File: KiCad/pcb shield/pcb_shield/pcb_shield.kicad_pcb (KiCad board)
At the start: 2 copper layers, 190 x 65 mm, 24 parts, among them J1 , J10 Motor Conn L, J11 Motor Conn R, J12 Endstop X, J13 Endstop Y, J2 , J3 , J4 , J5 , J6 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

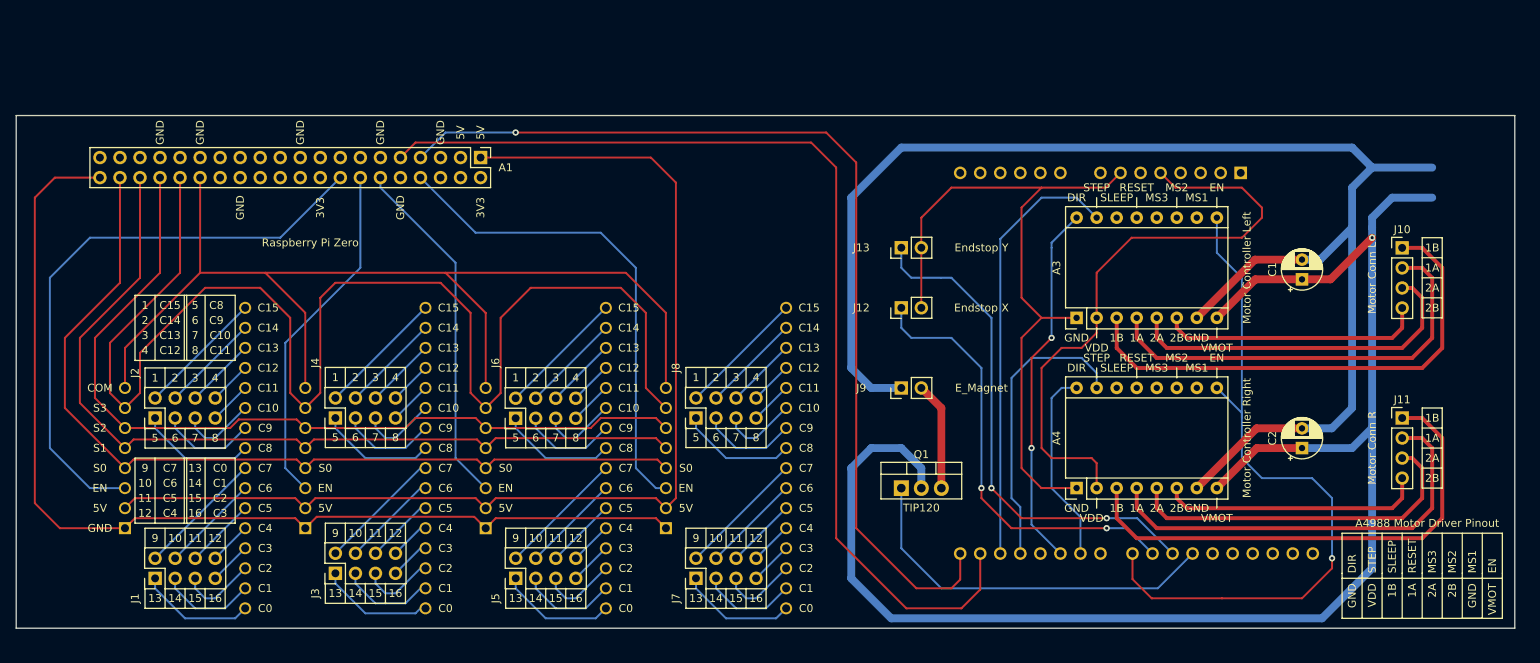
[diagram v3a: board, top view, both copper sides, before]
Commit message: add aditional headers
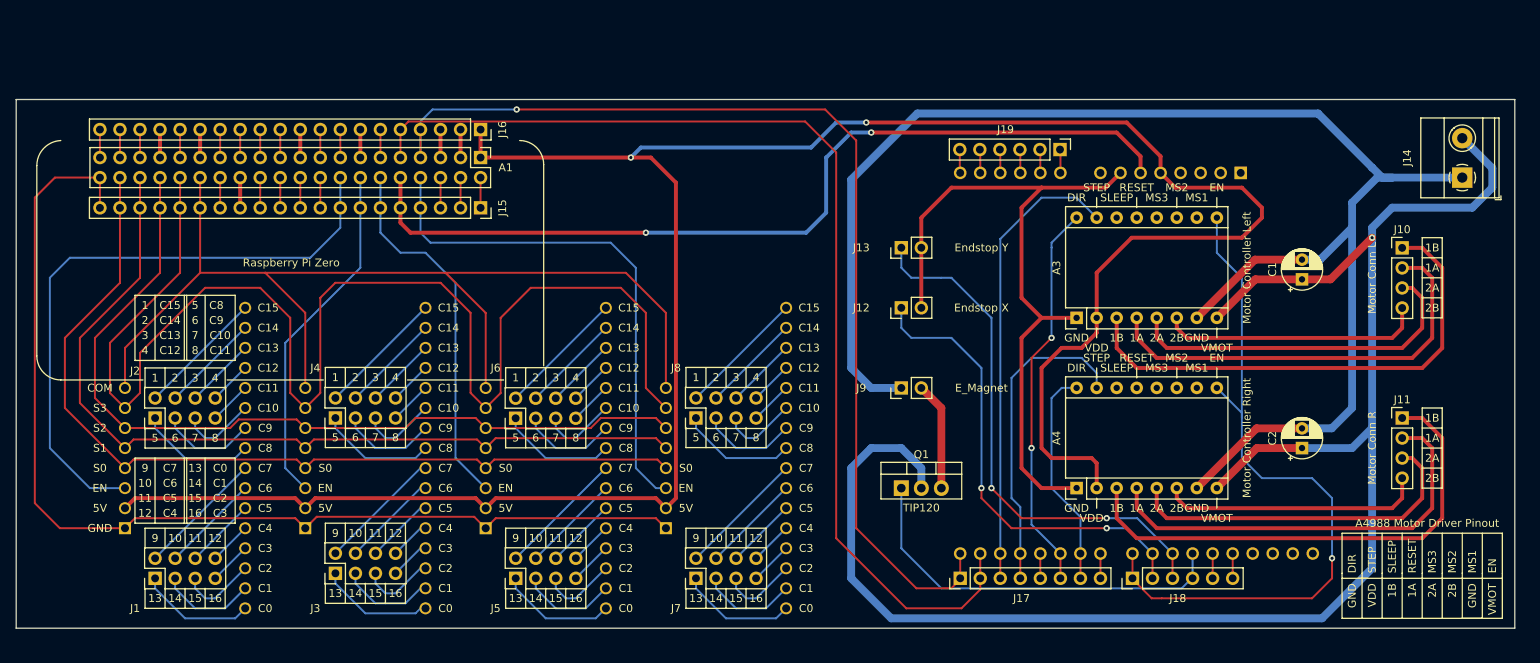
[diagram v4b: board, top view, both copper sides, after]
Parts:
- added J14: Barrel_Jack, TerminalBlock_Phoenix:TerminalBlock_Phoenix_MKDS-1,5-2_1x02_P5.00mm_Horizontal, F.Cu at (243.8, 71.1)
- added J15: Add Conn, Connector_PinSocket_2.54mm:PinSocket_1x20_P2.54mm_Vertical, F.Cu at (119.4, 75.0)
- added J16: Add Conn, Connector_PinSocket_2.54mm:PinSocket_1x20_P2.54mm_Vertical, F.Cu at (119.4, 65.0)
- added J17: Add Conn, Connector_PinHeader_2.54mm:PinHeader_1x08_P2.54mm_Vertical, F.Cu at (180.2, 121.9)
- added J18: Add Conn, Connector_PinHeader_2.54mm:PinHeader_1x06_P2.54mm_Vertical, F.Cu at (202.0, 121.9)
- added J19: Add Conn, Connector_PinHeader_2.54mm:PinHeader_1x06_P2.54mm_Vertical, F.Cu at (192.8, 67.6)
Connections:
- A1 pad 14: unconnected-(A1-Pad14) -> Net-(A1-Pad14)
- A1 pad 26: GND -> Net-(A1-Pad26)
- A1 pad 27: unconnected-(A1-Pad27) -> GND
- A1 pad 34: unconnected-(A1-Pad34) -> Net-(A1-Pad34)
- A2 pad 10: unconnected-(A2-Pad10) -> Net-(A2-Pad10)
- A2 pad 11: unconnected-(A2-Pad11) -> Net-(A2-Pad11)
- A2 pad 12: unconnected-(A2-Pad12) -> Net-(A2-Pad12)
- A2 pad 13: unconnected-(A2-Pad13) -> Net-(A2-Pad13)
- A2 pad 14: unconnected-(A2-Pad14) -> Net-(A2-Pad14)
- A2 pad 19: unconnected-(A2-Pad19) -> Net-(A2-Pad19)
- A2 pad 22: unconnected-(A2-Pad22) -> Net-(A2-Pad22)
- A2 pad 27: unconnected-(A2-Pad27) -> Net-(A2-Pad27)
- A2 pad 28: unconnected-(A2-Pad28) -> Net-(A2-Pad28)
- A2 pad 5: Net-(A4-Pad2) -> 5V
- A2 pad 6: unconnected-(A2-Pad6) -> GND
- A2 pad 9: unconnected-(A2-Pad9) -> Net-(A2-Pad9)
- A3 pad 2: Net-(A4-Pad2) -> 5V
- A4 pad 2: Net-(A4-Pad2) -> 5V
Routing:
- net 5V: track 139.6 -> 296.9 mm, vias 0 -> 2
- net GND: track 0.00 -> 134.4 mm, vias 0 -> 2
- net Net-(A4-Pad2): track 77.3 -> 0.00 mm
- net Net-(A3-Pad8): track 198.1 -> 213.4 mm
- net /14 TXD: track 124.6 -> 134.9 mm
- net Net-(A3-Pad7): track 186.2 -> 196.3 mm
- net 3V3: track 0.00 -> 7.67 mm
- net /18 RXD: track 131.8 -> 137.2 mm
- net Net-(A1-Pad4): track 62.3 -> 66.4 mm
- net SDA: track 0.00 -> 3.83 mm
- net SCL: track 0.00 -> 3.83 mm
- net Net-(A1-Pad14): track 0.00 -> 3.83 mm
- net 9 MISO: track 0.00 -> 3.83 mm
- net 11 SCLK: track 0.00 -> 3.83 mm
- net 10 MOSI: track 0.00 -> 3.83 mm
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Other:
- board size 190 x 65 mm -> 190 x 67 mm
- board text added: "17"
- board text added: "18"
- board text added: "19"
- board text added: "20"
- board text added: "21"
- board text added: "22"
- board text added: "23"
- board text added: "24"
- board text added: "25"
- board text added: "26"
- board text added: "27"
- board text added: "Arduino Uno"
- board text added: "RXD"
- board text added: "SCL"
- board text added: "SDA"
- board text added: "TXD"

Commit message: working on PCB and creating manufacturing files
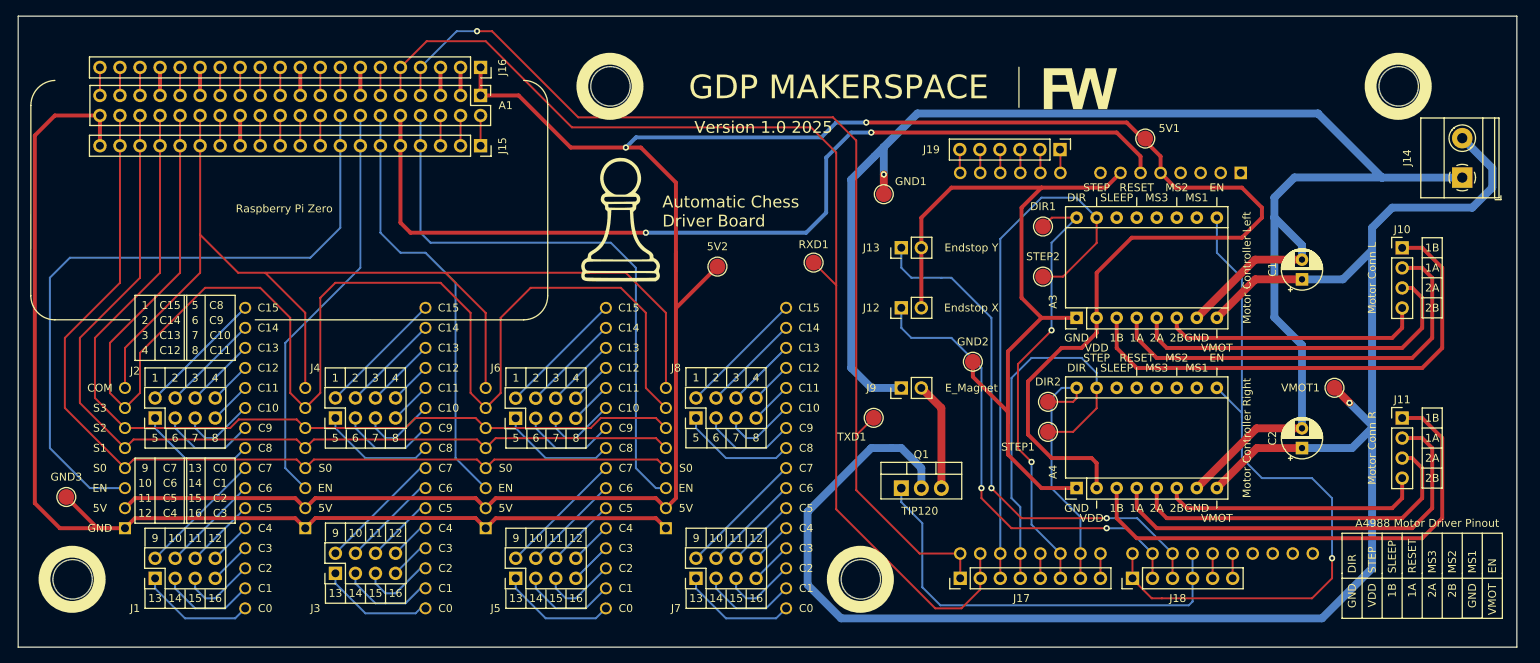
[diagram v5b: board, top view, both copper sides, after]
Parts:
- added 5V1: 5V, TestPoint:TestPoint_Pad_D2.0mm, F.Cu at (203.7, 66.2)
- added 5V2: 5V, TestPoint:TestPoint_Pad_D2.0mm, F.Cu at (149.4, 82.4)
- added DIR1: DIR, TestPoint:TestPoint_Pad_D2.0mm, F.Cu at (190.7, 77.3)
- added DIR2: DIR, TestPoint:TestPoint_Pad_D2.0mm, F.Cu at (191.3, 99.5)
- added GND1: GND, TestPoint:TestPoint_Pad_D2.0mm, F.Cu at (170.5, 73.2)
- added GND2: GND, TestPoint:TestPoint_Pad_D2.0mm, F.Cu at (181.8, 94.5)
- added GND3: GND, TestPoint:TestPoint_Pad_D2.0mm, F.Cu at (66.9, 111.6)
- added RXD1: RXD, TestPoint:TestPoint_Pad_D2.0mm, F.Cu at (161.6, 81.9)
- added STEP1: STEP, TestPoint:TestPoint_Pad_D2.0mm, F.Cu at (191.3, 103.4)
- added STEP2: STEP, TestPoint:TestPoint_Pad_D2.0mm, F.Cu at (190.7, 83.7)
- added TXD1: TXD, TestPoint:TestPoint_Pad_D2.0mm, F.Cu at (169.2, 101.6)
- added VMOT1: VMOT, TestPoint:TestPoint_Pad_D2.0mm, F.Cu at (227.6, 97.8)
- C1, C2: value C -> 100uF
- moved J16 7.87 mm to (119.4, 57.1)
- moved A1 7.87 mm to (119.4, 60.7)
- moved J15 7.87 mm to (119.4, 67.1)
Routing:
- net Net-(A3-Pad8): track 213.4 -> 228.1 mm
- net Net-(A1-Pad20): track 136.5 -> 151.1 mm
- net 5V: track 296.9 -> 311.4 mm
- net Net-(A2-Pad17): track 58.5 -> 70.2 mm
- net Net-(A2-Pad7): track 90.2 -> 101.1 mm
- net Net-(A3-Pad7): track 196.3 -> 206.4 mm, vias 0 -> 1
- net Net-(A2-Pad18): track 40.4 -> 50.4 mm
- net Net-(A1-Pad15): track 134.7 -> 144.6 mm
- net GND: track 134.4 -> 142.3 mm
- net Net-(A1-Pad16): track 173.4 -> 181.3 mm
- net Net-(A1-Pad4): track 66.4 -> 74.3 mm
- net Net-(A1-Pad18): track 111.2 -> 119.1 mm
- net Net-(A1-Pad17): track 108.3 -> 116.2 mm
- net Net-(A1-Pad7): track 44.4 -> 52.2 mm
- net Net-(A1-Pad6): track 46.8 -> 54.6 mm
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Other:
- board size 190 x 67 mm -> 190 x 80 mm
- board text added: "Automatic Chess Driver Board"
- board text added: "GDP MAKERSPACE"
- board text added: "Version 1.0 2025"

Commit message: make files for hackclub pcb grant
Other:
- board text added: "FW"
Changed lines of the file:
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@@
   (gr_line (start 99.69 105.41) (end 99.69 103.12) (layer "F.SilkS") (width 0.15))
   (gr_line (start 155.57 95.22) (end 155.57 97.54) (layer "F.SilkS") (width 0.15))
-  (gr_poly
-    (pts
-      (xy 195.128 60.813)
-      (xy 196.075301 57.254499)
-      (xy 197.319186 57.254499)
-      (xy 198.227364 60.873074)
-      (xy 199.022461 57.254499)
-      (xy 200.075524 57.254499)
-      (xy 198.817503 62.434999)
-      (xy 197.707901 62.434999)
-      (xy 196.676041 58.561992)
-      (xy 195.647463 62.434998)
-      (xy 194.513125 62.434998)
-      (xy 193.987604 60.233463)
-      (xy 191.88695 60.233463)
-      (xy 191.88695 62.434998)
-      (xy 190.789799 62.434998)
-      (xy 190.789799 59.357089)
-      (xy 191.88695 59.357089)
-      (xy 193.778354 59.357089)
-      (xy 193.536714 58.130872)
-      (xy 191.88695 58.130872)
-      (xy 191.88695 59.357089)
-      (xy 190.789799 59.357089)
-      (xy 190.789799 57.254499)
-      (xy 194.347038 57.254499)
-    ) (layer "F.SilkS") (width 0) (fill solid))
   (gr_line (start 207.645 96.1952) (end 207.645 95.25) (layer "F.SilkS") (width 0.15))
   (gr_line (start 76.835 95.25) (end 86.995 95.25) (layer "F.SilkS") (width 0.15))
@@
   (gr_text "MS3" (at 205.105 73.66) (layer "F.SilkS")
     (effects (font (size 1 1) (thickness 0.15)))
+  )
+  (gr_text "FW" (at 194.078 59.783) (layer "F.SilkS")
+    (effects (font (size 4 4) (thickness 1)))
   )
   (gr_text "2" (at 103.5 96.52) (layer "F.SilkS")
@@
     )
   )
-  (group "" (id dce69519-c1cf-483b-b75c-37fcb61ba768)
-    (members
-      ad39c230-9f13-46a2-89b6-387a4b1f0bc6
-    )
-  )
